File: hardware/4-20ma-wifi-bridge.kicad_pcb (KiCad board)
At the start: 2 copper layers, 32 x 83 mm, 16 parts, among them J1 Conn_01x19_Female, J2 Conn_01x19_Female, J3 Screw_Terminal_01x02, J4 Screw_Terminal_01x02, M1 DC-DC_Buck_Step_Module-dc-dc_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, SW1 SW_DIP_x01, U1 ESP32-DEVKITC-32D, U2 INA196

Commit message: Added kicad design files
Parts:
- added D2: LED, LED_THT:LED_D3.0mm_FlatTop, F.Cu at (145.3, 47.6)
- added D3: 1N4004, Diode_SMD:D_SMA, F.Cu at (151.0, 73.4)
- added D4: 1N4004, Diode_SMD:D_SMA, F.Cu at (142.5, 73.4)
- added D5: LED, LED_THT:LED_D1.8mm_W1.8mm_H2.4mm_Horizontal_O1.27mm_Z1.6mm, F.Cu at (158.6, 119.7)
- added J3: Screw_Terminal_01x02, project_library:TerminalBlock__1x02_P5.00mm_90Degree, F.Cu at (160.9, 43.4)
- added J4: Screw_Terminal_01x02, project_library:TerminalBlock__1x02_P5.00mm_90Degree, F.Cu at (149.3, 43.4)
- added K1: G5V-1, Relay_THT:Relay_SPDT_Omron_G5V-1, F.Cu at (153.6, 68.3)
- added K2: G5V-1, Relay_THT:Relay_SPDT_Omron_G5V-1, F.Cu at (144.9, 68.3)
- added Q1: 2N7002E, Package_TO_SOT_SMD:SOT-23, F.Cu at (149.9, 77.6)
- added Q2: 2N7002E, Package_TO_SOT_SMD:SOT-23, F.Cu at (141.4, 77.6)
- added R1: 1k, Resistor_SMD:R_0805_2012Metric_Pad1.20x1.40mm_HandSolder, F.Cu at (141.3, 80.9)
- added R2: 1k, Resistor_SMD:R_0805_2012Metric_Pad1.20x1.40mm_HandSolder, F.Cu at (149.8, 80.9)
- added R3: 1k, Resistor_SMD:R_0805_2012Metric_Pad1.20x1.40mm_HandSolder, F.Cu at (158.6, 51.1)
- added R4: 10k, Resistor_SMD:R_0805_2012Metric_Pad1.20x1.40mm_HandSolder, F.Cu at (153.2, 77.6)
- added R5: 1k, Resistor_SMD:R_0805_2012Metric_Pad1.20x1.40mm_HandSolder, F.Cu at (146.8, 51.1)
- added R6: 10k, Resistor_SMD:R_0805_2012Metric_Pad1.20x1.40mm_HandSolder, F.Cu at (144.9, 77.6)
- added TP1: TestPoint, TestPoint:TestPoint_Pad_D1.0mm, F.Cu at (158.6, 108.8)
- added TP2: TestPoint, TestPoint:TestPoint_Pad_D1.0mm, F.Cu at (158.6, 112.7)
- added TP3: TestPoint, TestPoint:TestPoint_Pad_D1.0mm, F.Cu at (176.1, 55.3)
- D1: footprint LED_THT:LED_D1.8mm_W1.8mm_H2.4mm_Horizontal_O1.27mm_Z4.9mm -> LED_THT:LED_D3.0mm_FlatTop
- R10: renamed from R4; value 4.99 -> 2.7ohm; footprint Resistor_SMD:R_0805_2012Metric_Pad1.20x1.40mm_HandSolder -> Resistor_SMD:R_2512_6332Metric_Pad1.40x3.35mm_HandSolder
- R7: renamed from R1; value 250 -> 1k
- R8: renamed from R2; value 250 -> 1k
- R9: renamed from R3; value 4.99 -> 10k
- U1: value ESP32-DEVKITC-32D -> ESP32-DEVKITC-32U; footprint project_library:MODULE_ESP32-DEVKITC-32D -> project_library:MODULE_ESP32-DEVKITC-32U
- U2: value INA196 -> LMP8640; footprint Package_TO_SOT_SMD:SOT-23-5 -> Package_TO_SOT_SMD:SOT-23-6
- moved U1 108.0 mm to (217.6, 82.7)
- moved SW1 78.9 mm to (178.0, 120.2), turned to 180 degrees
- moved D1 73.3 mm to (157.0, 47.6)
- moved R9 57.1 mm to (175.8, 114.2), turned to 0 degrees
- moved R10 30.0 mm to (175.1, 48.3)
- moved U2 29.7 mm to (175.1, 52.4), turned to 180 degrees
- moved J6 26.7 mm to (177.7, 43.4)
- moved C1 24.3 mm to (171.8, 52.3)
- moved J1 15.5 mm to (156.8, 58.4)
- moved J2 15.5 mm to (182.2, 58.4)
- moved H1 13.5 mm to (178.5, 107.0)
- moved M1 6.58 mm to (138.2, 111.3)
- moved D6 1.56 mm to (164.3, 119.7)
- moved R7 1.56 mm to (162.1, 117.2)
- moved R8 1.56 mm to (165.8, 117.2)
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- renumbered D2 to D6, J3 to J5, J4 to J6
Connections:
- D1 pad 1: led1 -> Net-(D1-Pad1)
- J1 pad 10: unconnected-(J1-Pad10) -> relay1
- J1 pad 11: unconnected-(J1-Pad11) -> relay2
- J1 pad 3: unconnected-(J1-Pad3) -> vsens
- J1 pad 5: vsens -> unconnected-(J1-Pad5)
- J2 pad 10: led2 -> unconnected-(J2-Pad10)
- J2 pad 17: unconnected-(J2-Pad17) -> led1
- J2 pad 18: unconnected-(J2-Pad18) -> led2
- J2 pad 19: unconnected-(J2-Pad19) -> switch
- J2 pad 2: switch -> unconnected-(J2-Pad2)
- J2 pad 9: led1 -> unconnected-(J2-Pad9)
- J6 pad 1: Net-(R4-Pad1) -> Net-(J6-Pad1)
- J6 pad 2: Net-(J4-Pad2) -> Net-(J6-Pad2)
- R10 pad 1: Net-(R4-Pad1) -> Net-(J6-Pad1)
- R10 pad 2: Net-(J4-Pad2) -> Net-(J6-Pad2)
- R7 pad 1: Net-(D1-Pad2) -> Net-(D5-Pad2)
- U2 pad 3: +5V -> Net-(J6-Pad1)
- U2 pad 4: Net-(R4-Pad1) -> Net-(J6-Pad2)
- U2 pad 5: Net-(J4-Pad2) -> (no net)
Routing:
- net +5V: track 54.6 -> 126.5 mm, vias 1 -> 3
- net Net-(D1-Pad1): track 0.00 -> 39.7 mm, vias 0 -> 1
- net Net-(D2-Pad1): track 0.00 -> 38.4 mm, vias 0 -> 1
- net Net-(J3-Pad2): track 0.00 -> 28.9 mm
- net Net-(J3-Pad1): track 0.00 -> 24.5 mm
- net Net-(J4-Pad1): track 0.00 -> 22.2 mm
- net Net-(R4-Pad1): track 20.3 -> 0.00 mm
- net vsens: track 6.80 -> 24.8 mm
- net relay2: track 0.00 -> 15.6 mm
- net +3V3: track 100.1 -> 85.8 mm
- net led2: track 44.9 -> 32.5 mm
- net led1: track 47.2 -> 36.3 mm
- net Net-(J6-Pad2): track 0.00 -> 10.0 mm
- net Net-(J6-Pad1): track 0.00 -> 9.86 mm
- net Net-(Q2-Pad1): track 0.00 -> 6.35 mm
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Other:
- board size 32 x 83 mm -> 46 x 82 mm
- board text added: "4-20mA Wifi bridge"
- board text added: "GND"
- board text added: "VCC"
- board text added: "by @metalzonix"

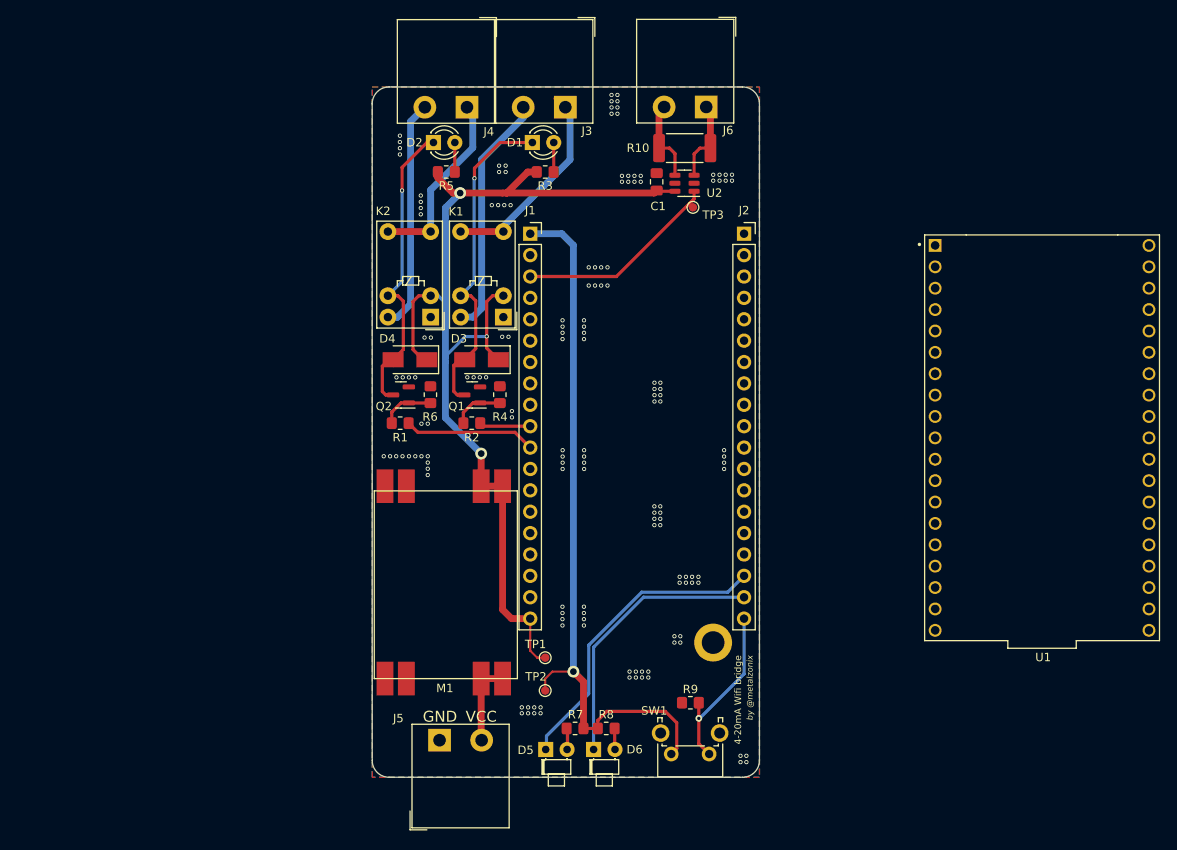
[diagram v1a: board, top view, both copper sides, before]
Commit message: Updated schematic and board to fix some erros
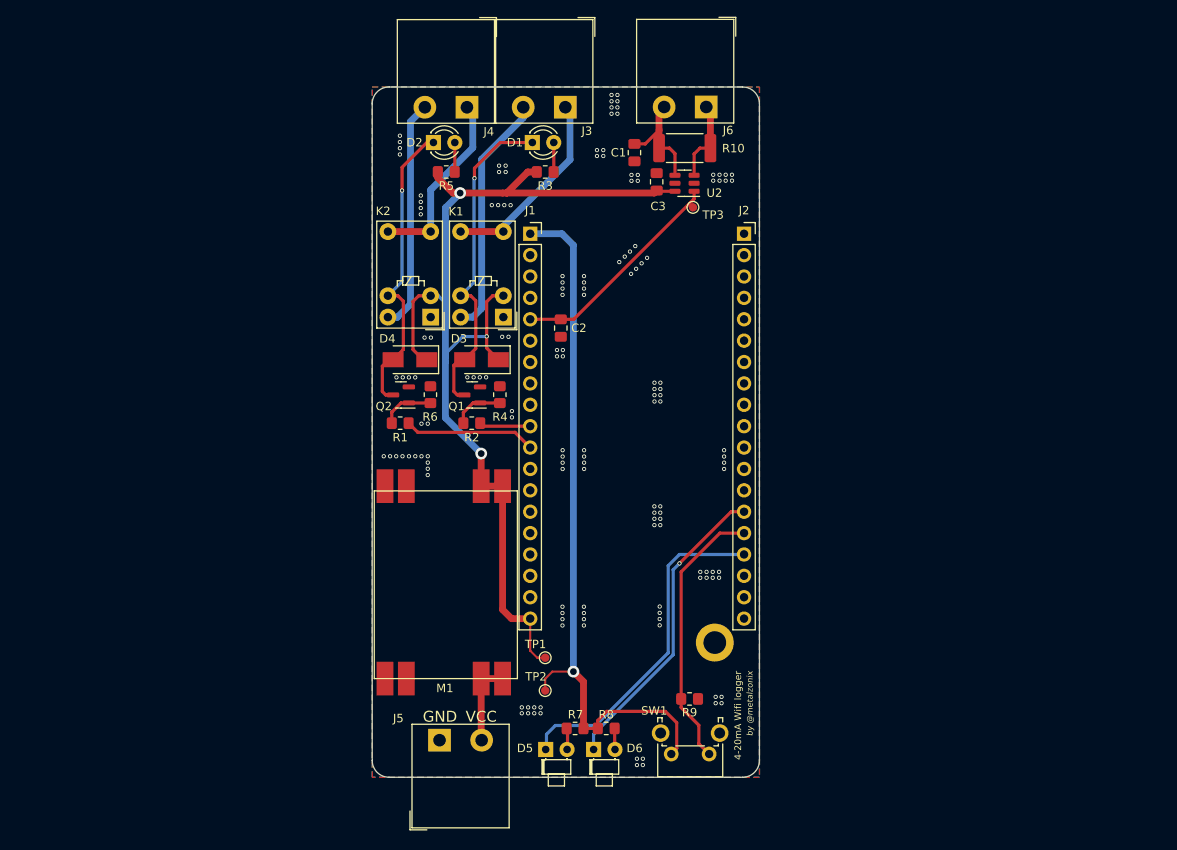
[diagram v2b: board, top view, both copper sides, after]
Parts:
- removed U1: ESP32-DEVKITC-32U, project_library:MODULE_ESP32-DEVKITC-32U
- added C1: 10 uF, Capacitor_SMD:C_0805_2012Metric_Pad1.18x1.45mm_HandSolder, F.Cu at (169.2, 48.8)
- added C2: 10 uF, Capacitor_SMD:C_0805_2012Metric_Pad1.18x1.45mm_HandSolder, F.Cu at (160.4, 69.6)
- moved R9 0.46 mm to (175.7, 113.7), turned to 180 degrees
- moved H1 0.20 mm to (178.7, 107.0)
- renumbered C1 to C3
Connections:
- J1 pad 3: vsens -> unconnected-(J1-Pad3)
- J1 pad 5: unconnected-(J1-Pad5) -> vsens
- J2 pad 14: unconnected-(J2-Pad14) -> led2
- J2 pad 15: unconnected-(J2-Pad15) -> switch
- J2 pad 16: unconnected-(J2-Pad16) -> led1
- J2 pad 17: led1 -> unconnected-(J2-Pad17)
- J2 pad 18: led2 -> unconnected-(J2-Pad18)
- J2 pad 19: switch -> unconnected-(J2-Pad19)
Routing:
- net switch: track 20.8 -> 32.4 mm, vias 1 -> 0
- net led2: track 32.5 -> 36.5 mm, vias 0 -> 1
- net led1: track 36.3 -> 40.2 mm
- net Net-(C1-Pad1): track 10.0 -> 13.6 mm
- net vsens: track 24.8 -> 26.9 mm
- net Net-(D2-Pad1): track 38.4 -> 36.5 mm
- net Net-(J3-Pad1): track 24.5 -> 23.4 mm
- net Net-(D1-Pad1): track 39.7 -> 39.0 mm
- net Net-(D5-Pad2): track 2.52 -> 3.13 mm
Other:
- board text added: "4-20mA Wifi logger"
- board text removed: "4-20mA Wifi bridge"
